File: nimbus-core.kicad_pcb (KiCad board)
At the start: 4 copper layers, 66 x 66 mm, 71 parts, among them J1 QTE-020-03-L-D-A, J2 QSE-020-01-L-D-A, J3 532614006, J4 USB4105-GF-A-120, J5 532614006, J6 532614006, U1 STM32F405VGT7, U10 Yellow, U4 SN65HVD233-Q1, U8 SN65HVD1782-Q1, U9 USBLC6-2P6, Y1 25MHz

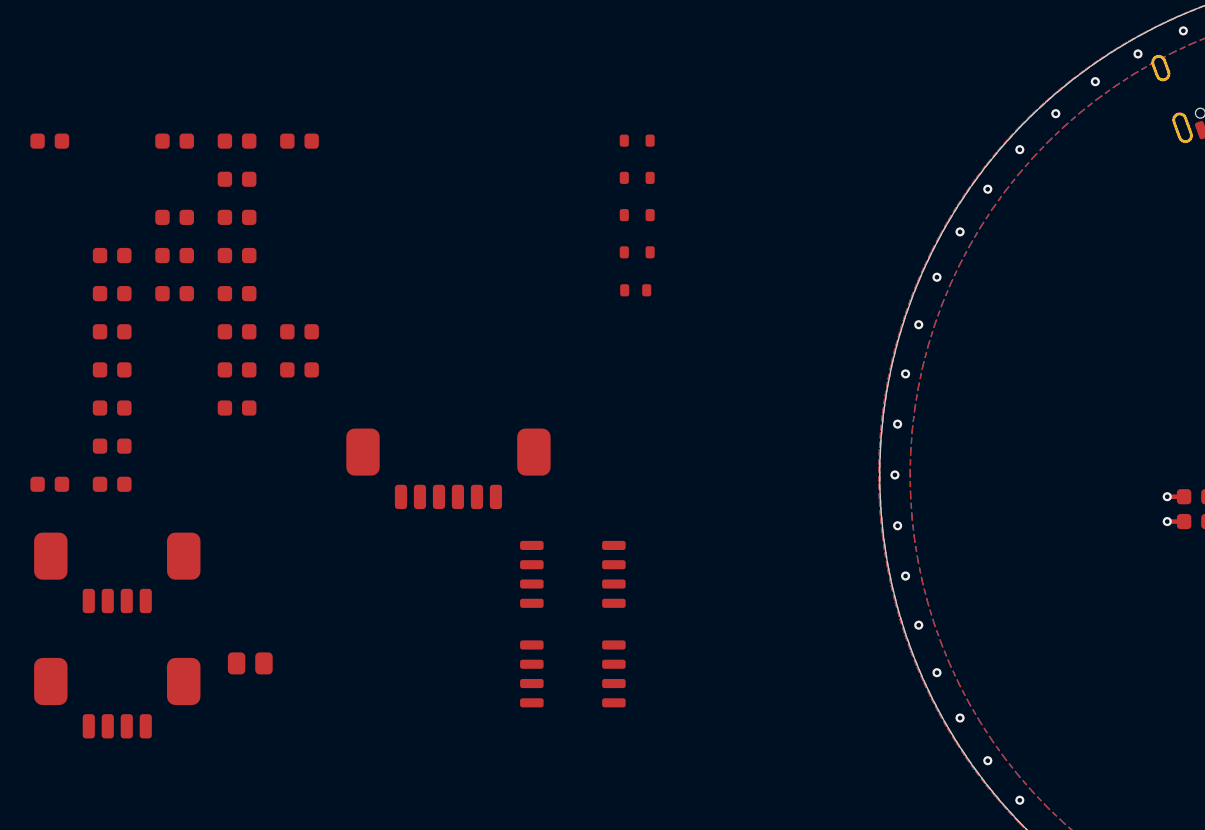
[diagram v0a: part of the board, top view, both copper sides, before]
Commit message: Place connectors around PCB edge
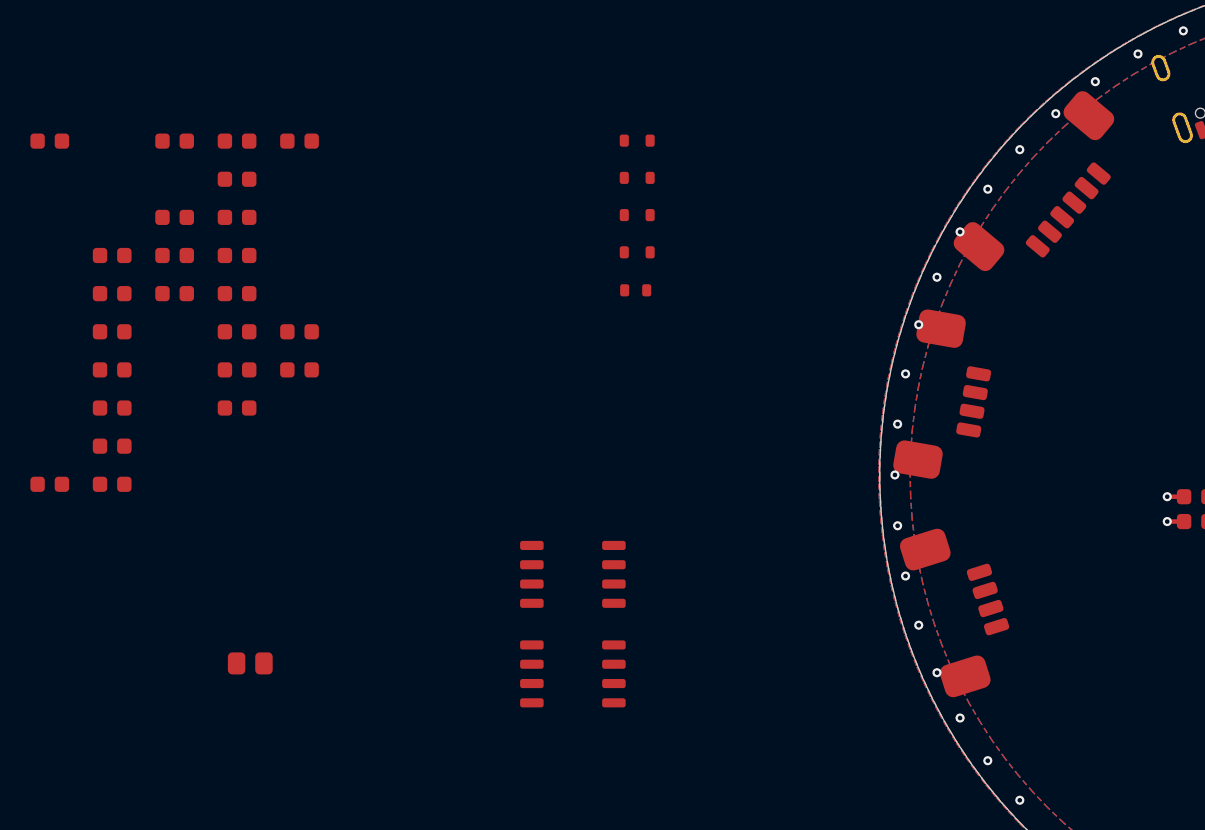
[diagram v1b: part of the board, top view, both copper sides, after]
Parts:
- moved J6 57.5 mm to (119.4, 99.8), turned to 80 degrees
- moved J3 55.2 mm to (120.4, 113.9), turned to 107.5 degrees
- moved J5 43.0 mm to (126.1, 86.1), turned to 50 degrees

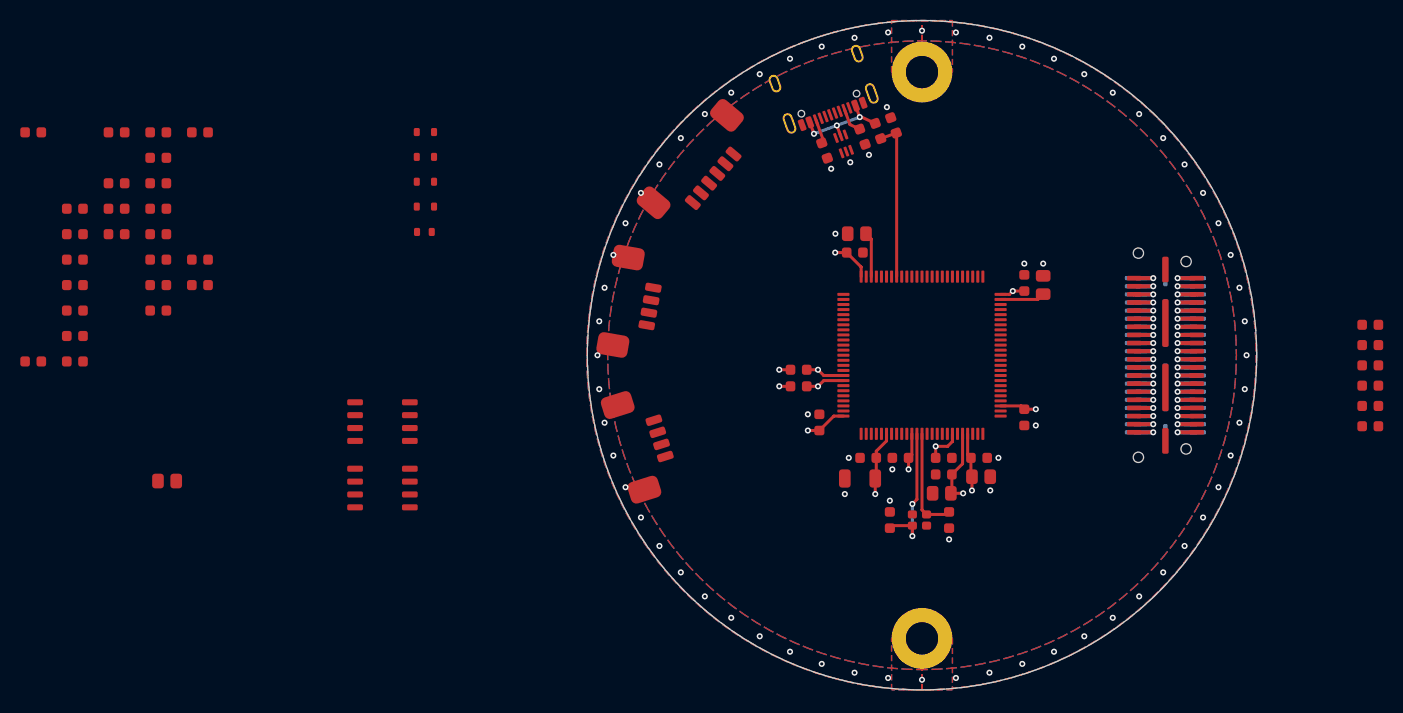
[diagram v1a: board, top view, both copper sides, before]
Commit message: Add TVS diodes to SWD connector
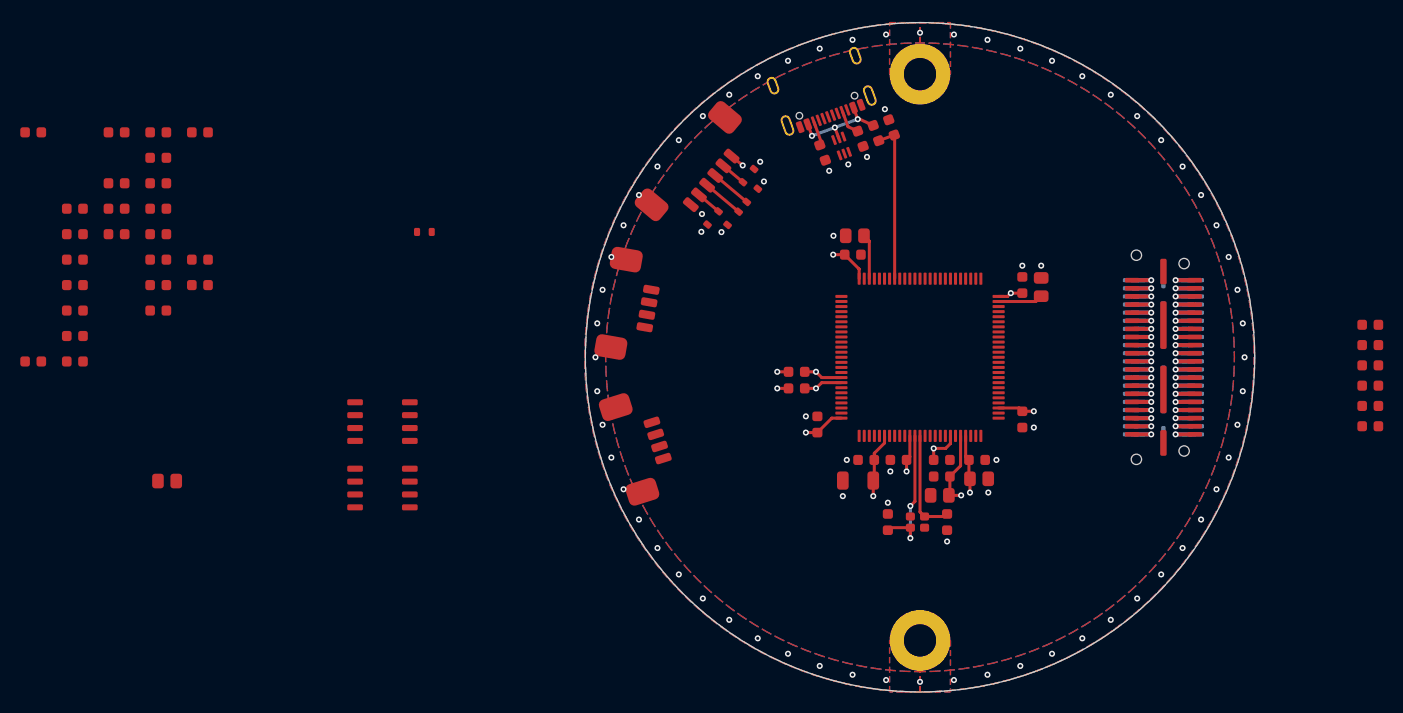
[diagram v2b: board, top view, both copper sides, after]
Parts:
- moved D2 32.5 mm to (131.8, 89.2), turned to 50 degrees
- moved D1 32.1 mm to (131.4, 87.3), turned to 50 degrees
- moved D3 30.5 mm to (129.9, 91.5), turned to -130 degrees
- moved D4 28.4 mm to (127.9, 91.5), turned to -130 degrees
- moved C16 0.28 mm to (141.7, 95.1)
- moved C19 0.28 mm to (142.2, 117.4)
- moved REF** 0.28 mm to (148.3, 77.3)
- moved Y1 0.28 mm to (148.1, 121.5)
- moved C14 0.28 mm to (150.3, 118.8)
- moved R19 0.28 mm to (136.1, 106.6)
- moved R20 0.28 mm to (136.1, 108.3)
- moved R22 0.28 mm to (142.4, 83.7)
- moved R25 0.28 mm to (138.7, 85.0)
- moved J3 0.28 mm to (120.2, 114.1)
- moved J5 0.28 mm to (126.0, 86.3)
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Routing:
- net /SWCLK: track 0.00 -> 4.05 mm
- net /SWO: track 0.00 -> 4.05 mm
- net /~{MCU_RESET}: track 0.00 -> 2.52 mm
- net /SWDIO: track 0.00 -> 2.52 mm
- net +3.3V: track 43.6 -> 45.0 mm, vias 11 -> 12
- net GND: vias 16 -> 21

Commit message: Switched PCB from round to octagonal
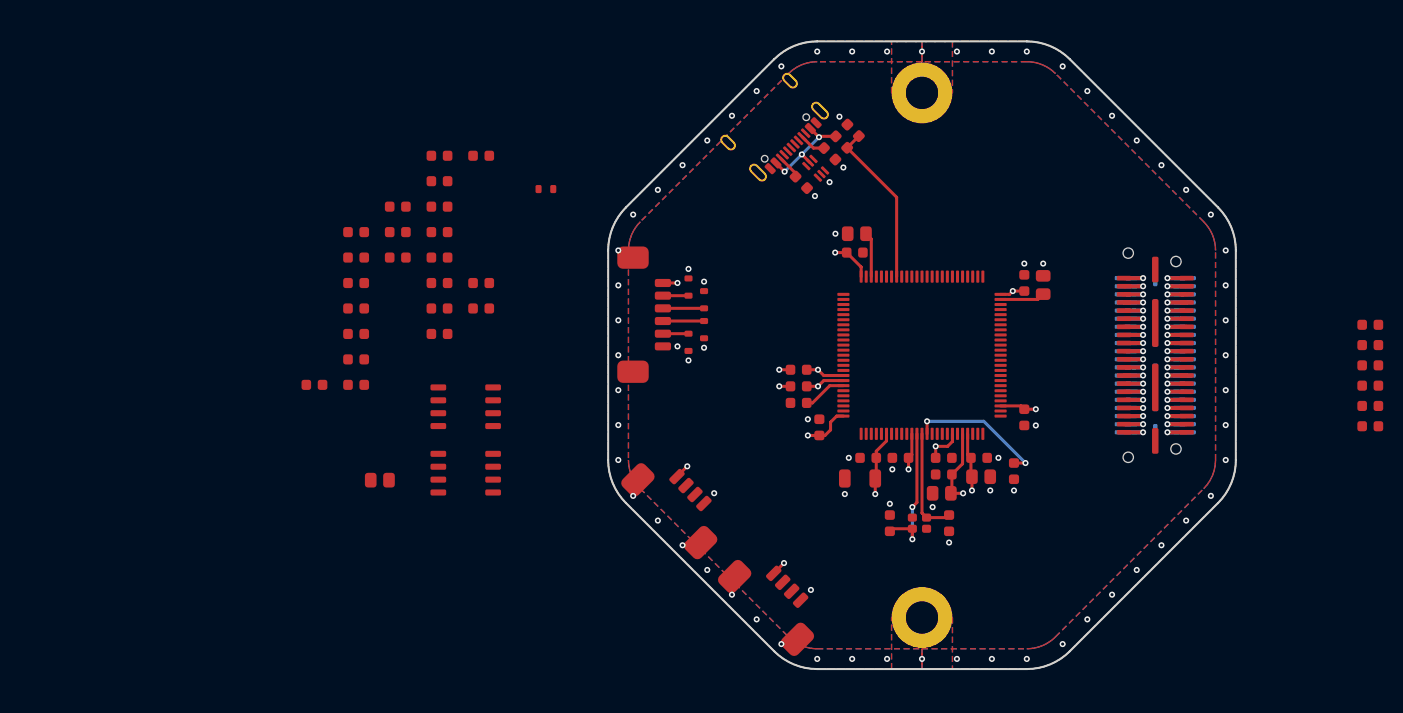
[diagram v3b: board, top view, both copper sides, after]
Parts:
- removed the REF** at (148.3, 133.1)
- removed the REF** at (148.3, 77.3)
- added REF**: Mounting_Hole_M3, layout:Mounting_Hole_M3, F.Cu at (148.5, 130.9)
- added REF**: Mounting_Hole_M3, layout:Mounting_Hole_M3, F.Cu at (148.5, 79.1)
- moved C1 102.3 mm to (157.6, 116.4), turned to -90 degrees
- moved R1 72.3 mm to (136.3, 109.7), turned to 180 degrees
- moved R17 27.8 mm to (100.9, 100.4)
- moved R11 27.8 mm to (100.9, 85.3)
- moved R12 27.8 mm to (100.9, 87.8)
- moved R13 27.8 mm to (100.9, 90.4)
- moved R14 27.8 mm to (100.9, 92.9)
- moved R15 27.8 mm to (100.9, 95.4)
- moved R16 27.8 mm to (100.9, 97.9)
- moved R18 27.8 mm to (100.9, 102.9)
- moved C23 27.8 mm to (92.7, 100.4)
- moved C26 27.8 mm to (92.7, 107.9)
- moved R27 27.8 mm to (105.0, 100.4)
- moved C15 27.8 mm to (88.6, 107.9)
- moved C20 27.8 mm to (92.7, 92.9)
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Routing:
- net /~{MCU_RESET}: track 2.52 -> 16.3 mm, vias 0 -> 2
- net /BOOT0: track 0.00 -> 4.32 mm
- net +3.3V: track 45.0 -> 48.5 mm, vias 12 -> 14
- net /USB_VBUS: track 15.8 -> 16.4 mm
- net GND: vias 21 -> 25
- net CHASSIS: vias 60 -> 56
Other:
- board size 66 x 66 mm -> 61.9 x 61.9 mm

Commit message: Add first connections to passtrough, will likely need some iteration
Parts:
- moved R21 42.7 mm to (146.8, 94.1), turned to 90 degrees
- moved U10 35.5 mm to (146.8, 91.2), turned to -90 degrees
- moved U4 12.4 mm to (103.5, 122.5), turned to 180 degrees
- moved R22 0.64 mm to (139.9, 85.6)
- moved R24 0.64 mm to (141.0, 84.4)
- moved R25 0.64 mm to (137.1, 88.4)
- moved U9 0.64 mm to (138.5, 87.0)
- moved R23 0.64 mm to (142.2, 83.3)
- moved C16 0.45 mm to (141.4, 94.9)
- moved C5 0.45 mm to (141.6, 93.0)
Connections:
- J1 pad 20: /PASSTHROUGH_P20 -> /ACCEL_IRQ
- J1 pad 24: /PASSTHROUGH_P24 -> /IMU_IRQ
- J2 pad 20: /PASSTHROUGH_P20 -> /ACCEL_IRQ
- J2 pad 24: /PASSTHROUGH_P24 -> /IMU_IRQ
- R10 pad 2: /~{RADIO_SS} -> /PASSTHROUGH_P8
- R2 pad 2: /~{ACCEL_SS} -> /PASSTHROUGH_P22
- R6 pad 2: /~{BAR_SS} -> /PASSTHROUGH_P16
- R7 pad 2: /~{IMU_SS} -> /PASSTHROUGH_P14
- R8 pad 2: /~{MAG_SS} -> /PASSTHROUGH_P12
- R9 pad 2: /~{MEM_SS} -> /PASSTHROUGH_P10
- U1 pad 30: /SP1_SCK -> /PASSTHROUGH_P40
- U1 pad 31: /SP1_MISO -> /PASSTHROUGH_P38
- U1 pad 32: /SP1_MOSI -> /PASSTHROUGH_P36
- U1 pad 33: unconnected-(U1D-PC4-Pad33) -> /PASSTHROUGH_P34
- U1 pad 34: unconnected-(U1D-PC5-Pad34) -> /PASSTHROUGH_P32
- U1 pad 35: /SENSE_PYRO2 -> /PASSTHROUGH_P30
- U1 pad 36: /SENSE_PYRO1 -> /PASSTHROUGH_P28
- U1 pad 37: unconnected-(U1C-PB2-Pad37) -> /PASSTHROUGH_P26
- U1 pad 39: /~{ACCEL_SS} -> /PASSTHROUGH_P22
- U1 pad 41: unconnected-(U1F-PE10-Pad41) -> /PASSTHROUGH_P18
- U1 pad 42: /~{BAR_SS} -> /PASSTHROUGH_P16
- U1 pad 43: /~{IMU_SS} -> /PASSTHROUGH_P14
- U1 pad 44: /~{MAG_SS} -> /PASSTHROUGH_P12
- U1 pad 45: /~{MEM_SS} -> /PASSTHROUGH_P10
- U1 pad 46: /~{RADIO_SS} -> /PASSTHROUGH_P8
- U1 pad 47: /RADIO_BUSY -> /PASSTHROUGH_P6
- U1 pad 48: /RADIO_IRQ -> /PASSTHROUGH_P4
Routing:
- net /IMU_IRQ: track 0.00 -> 16.2 mm, vias 0 -> 1
- net /ACCEL_IRQ: track 0.00 -> 16.0 mm, vias 0 -> 1
- net /PASSTHROUGH_P40: track 3.55 -> 17.2 mm
- net /PASSTHROUGH_P38: track 3.55 -> 17.1 mm
- net /PASSTHROUGH_P36: track 3.55 -> 17.0 mm
- net /PASSTHROUGH_P34: track 3.55 -> 16.8 mm
- net /PASSTHROUGH_P32: track 3.55 -> 16.7 mm
- net /PASSTHROUGH_P30: track 3.55 -> 16.6 mm
- net /PASSTHROUGH_P28: track 3.55 -> 16.5 mm
- net /PASSTHROUGH_P4: track 3.55 -> 16.5 mm
- net /PASSTHROUGH_P6: track 3.55 -> 16.3 mm
- net /PASSTHROUGH_P26: track 3.55 -> 16.3 mm
- net /PASSTHROUGH_P8: track 3.55 -> 16.2 mm
- net /PASSTHROUGH_P10: track 3.55 -> 16.1 mm
- net /PASSTHROUGH_P22: track 3.55 -> 16.1 mm
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
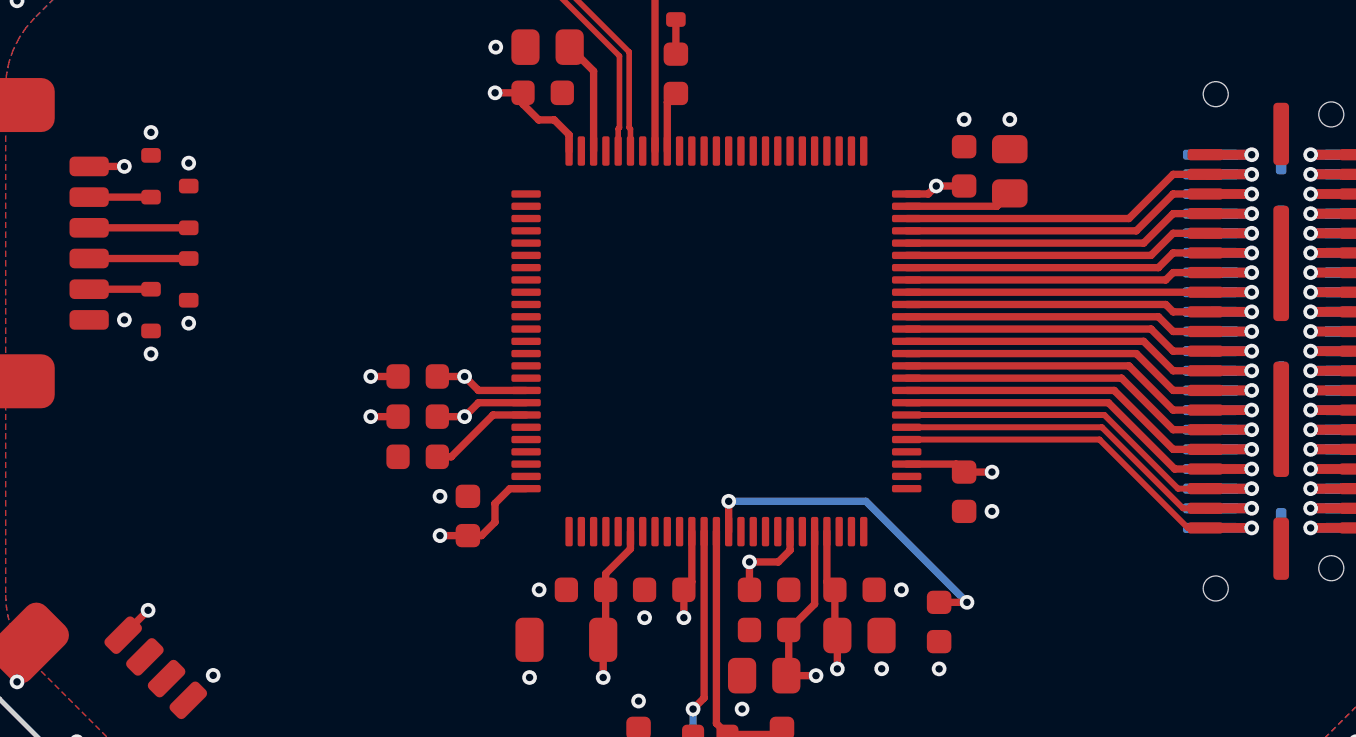
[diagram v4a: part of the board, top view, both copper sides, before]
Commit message: Shift passthrough pinout by 1 to insert another pin
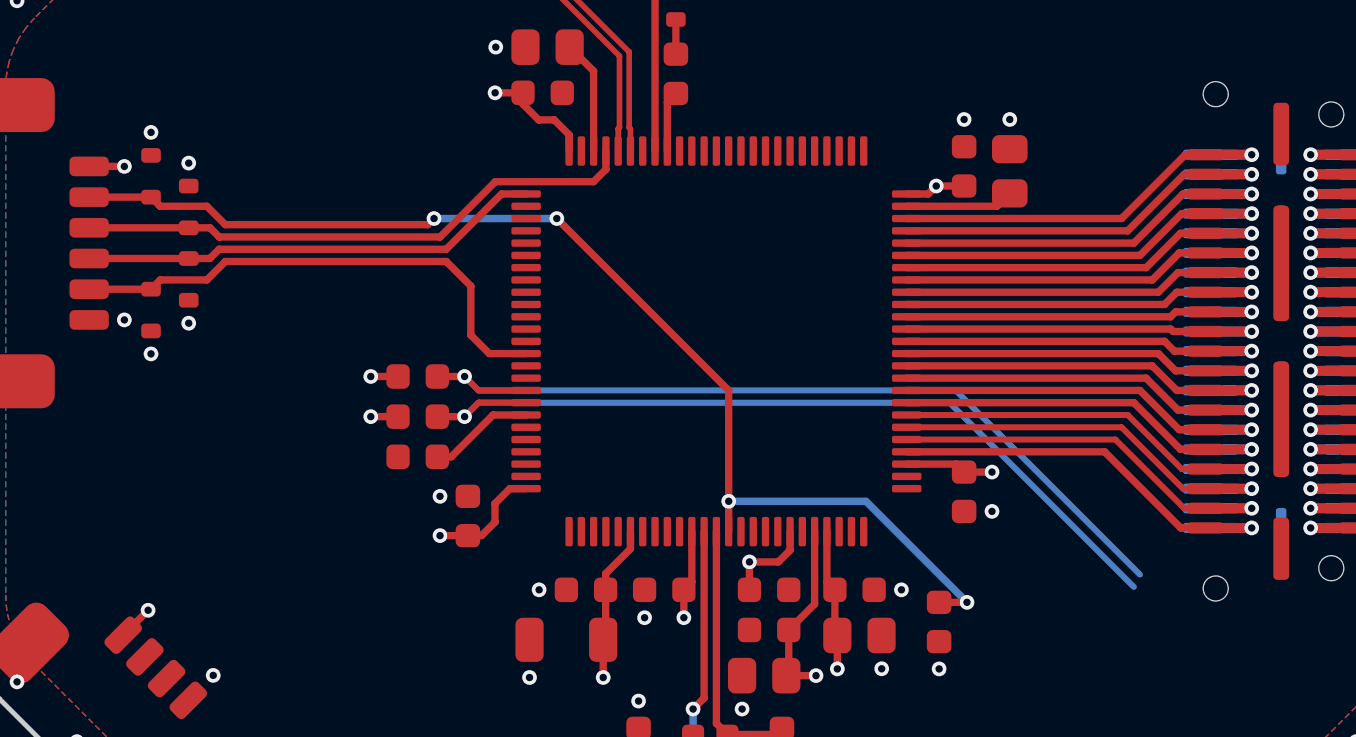
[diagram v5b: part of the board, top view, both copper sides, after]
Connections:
- D2 pad 1: /SWO -> /SWDIO
- D4 pad 1: /SWDIO -> /SWO
- J1 pad 18: /PASSTHROUGH_P18 -> /ACCEL_IRQ
- J1 pad 20: /ACCEL_IRQ -> /PASSTHROUGH_P20
- J1 pad 22: /PASSTHROUGH_P22 -> /IMU_IRQ
- J1 pad 24: /IMU_IRQ -> /PASSTHROUGH_P24
- J2 pad 18: /PASSTHROUGH_P18 -> /ACCEL_IRQ
- J2 pad 20: /ACCEL_IRQ -> /PASSTHROUGH_P20
- J2 pad 22: /PASSTHROUGH_P22 -> /IMU_IRQ
- J2 pad 24: /IMU_IRQ -> /PASSTHROUGH_P24
- J5 pad 3: /SWO -> /SWDIO
- J5 pad 5: /SWDIO -> /SWO
- R10 pad 2: /PASSTHROUGH_P8 -> /PASSTHROUGH_P6
- R2 pad 2: /PASSTHROUGH_P22 -> /PASSTHROUGH_P20
- R6 pad 2: /PASSTHROUGH_P16 -> /PASSTHROUGH_P14
- R7 pad 2: /PASSTHROUGH_P14 -> /PASSTHROUGH_P12
- R8 pad 2: /PASSTHROUGH_P12 -> /PASSTHROUGH_P10
- R9 pad 2: /PASSTHROUGH_P10 -> /PASSTHROUGH_P8
- U1 pad 29: unconnected-(U1B-PA4-Pad29) -> /PASSTHROUGH_P40
- U1 pad 30: /PASSTHROUGH_P40 -> /PASSTHROUGH_P38
- U1 pad 31: /PASSTHROUGH_P38 -> /PASSTHROUGH_P36
- U1 pad 32: /PASSTHROUGH_P36 -> /PASSTHROUGH_P34
- U1 pad 33: /PASSTHROUGH_P34 -> /PASSTHROUGH_P32
- U1 pad 34: /PASSTHROUGH_P32 -> /PASSTHROUGH_P30
- U1 pad 35: /PASSTHROUGH_P30 -> /PASSTHROUGH_P28
- U1 pad 36: /PASSTHROUGH_P28 -> /PASSTHROUGH_P26
- U1 pad 37: /PASSTHROUGH_P26 -> /PASSTHROUGH_P24
- U1 pad 39: /PASSTHROUGH_P22 -> /PASSTHROUGH_P20
- U1 pad 41: /PASSTHROUGH_P18 -> /PASSTHROUGH_P16
- U1 pad 42: /PASSTHROUGH_P16 -> /PASSTHROUGH_P14
- U1 pad 43: /PASSTHROUGH_P14 -> /PASSTHROUGH_P12
- U1 pad 44: /PASSTHROUGH_P12 -> /PASSTHROUGH_P10
- U1 pad 45: /PASSTHROUGH_P10 -> /PASSTHROUGH_P8
- U1 pad 46: /PASSTHROUGH_P8 -> /PASSTHROUGH_P6
- U1 pad 47: /PASSTHROUGH_P6 -> /PASSTHROUGH_P4
- U1 pad 48: /PASSTHROUGH_P4 -> /PASSTHROUGH_P2
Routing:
- net /~{MCU_RESET}: track 16.3 -> 47.8 mm, vias 2 -> 4
- net /I2C1_SCL: track 3.85 -> 34.7 mm
- net /I2C1_SDA: track 3.85 -> 34.4 mm
- net /SWDIO: track 2.52 -> 23.1 mm
- net /SWO: track 4.05 -> 21.0 mm
- net /PASSTHROUGH_P22: track 16.1 -> 0.00 mm, vias 1 -> 0
- net /PASSTHROUGH_P24: track 0.00 -> 16.0 mm, vias 0 -> 1
- net /PASSTHROUGH_P18: track 15.8 -> 0.00 mm, vias 1 -> 0
- net /PASSTHROUGH_P20: track 0.00 -> 15.8 mm, vias 0 -> 1
- net /SWCLK: track 4.06 -> 18.9 mm
- net /PASSTHROUGH_P2: track 3.55 -> 16.8 mm
